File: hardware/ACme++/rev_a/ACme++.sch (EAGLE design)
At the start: 92 parts, among them J1 AC-PLUG, J2 TC2030-CTX-NL, J3 WIRE_HOLE-14AWG, J4 WIRE_HOLE-14AWG, J5 WIRE_HOLE-14AWG, K1 S216S01F, Q1 STGD5NB120SZT4, Q2 FDV301N, U1 CC2538, U2 DS2411, U3 FM25LBTDFN-8, U4 ADE7753, U5 TXB0104RGY, U6 SR086SG-G, U7 TDA3664AT, X1 EPSON-FA-128, X2 FC-12M32.7680KA-A3, X3 ECS-35-17-5PX-TR

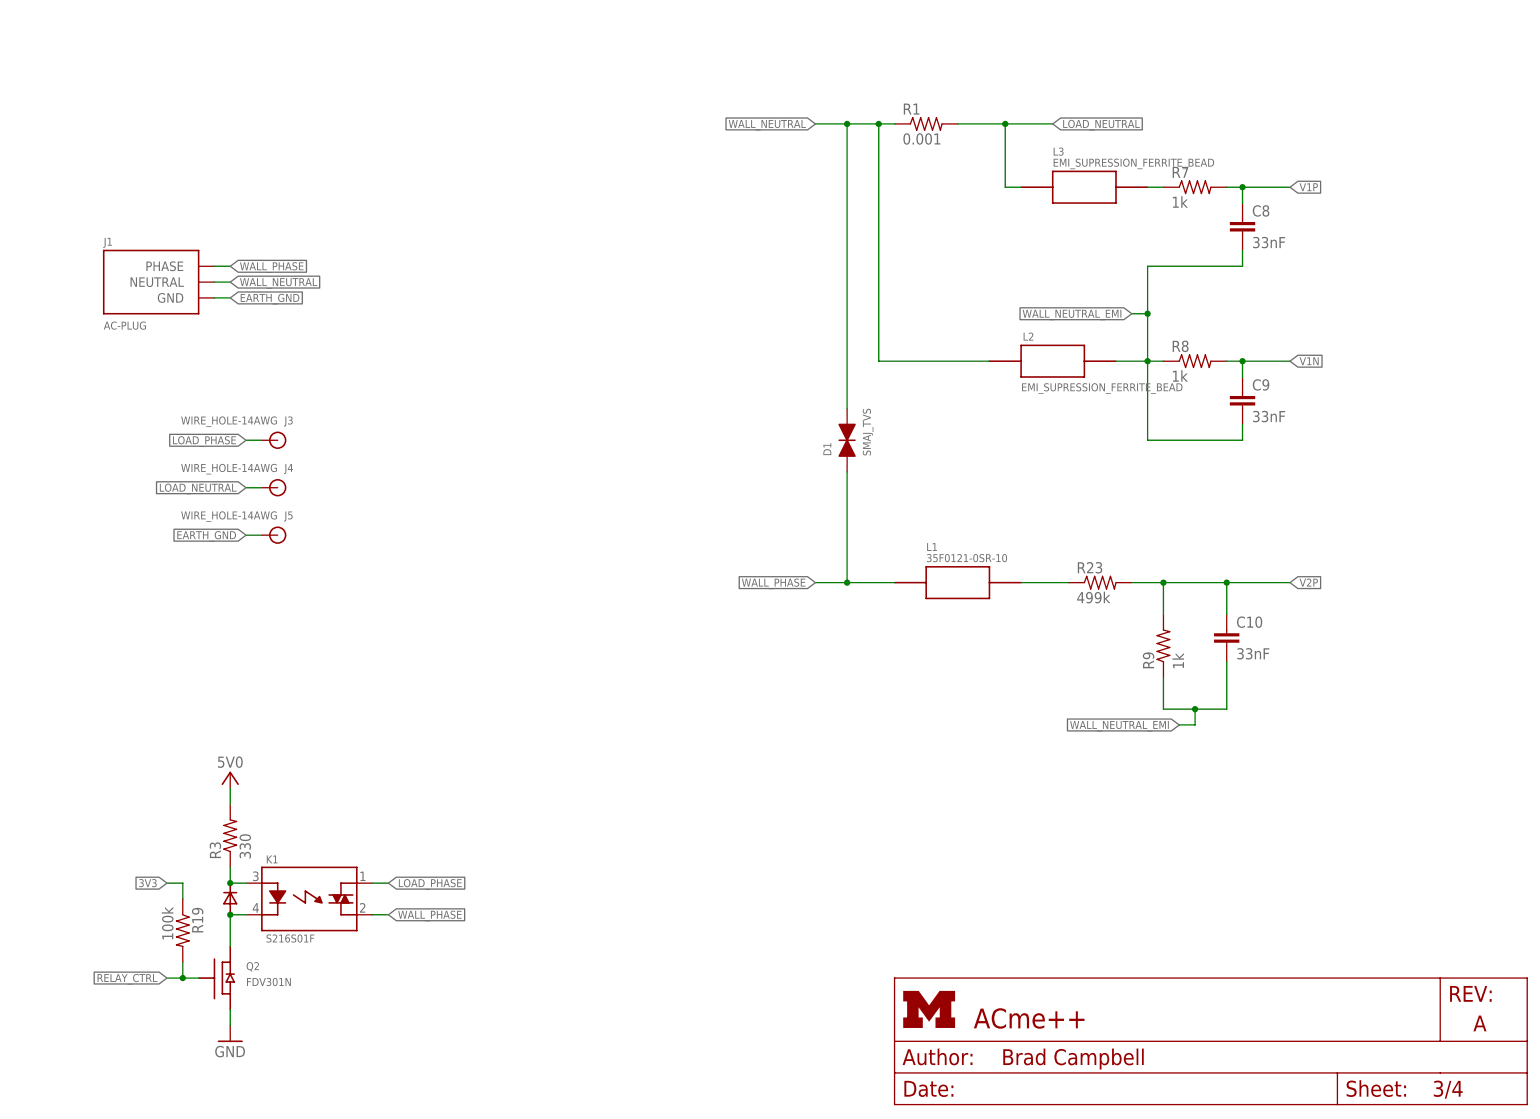
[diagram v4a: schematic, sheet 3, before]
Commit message: updates to acme++
- no plated earth gnd
- added test points
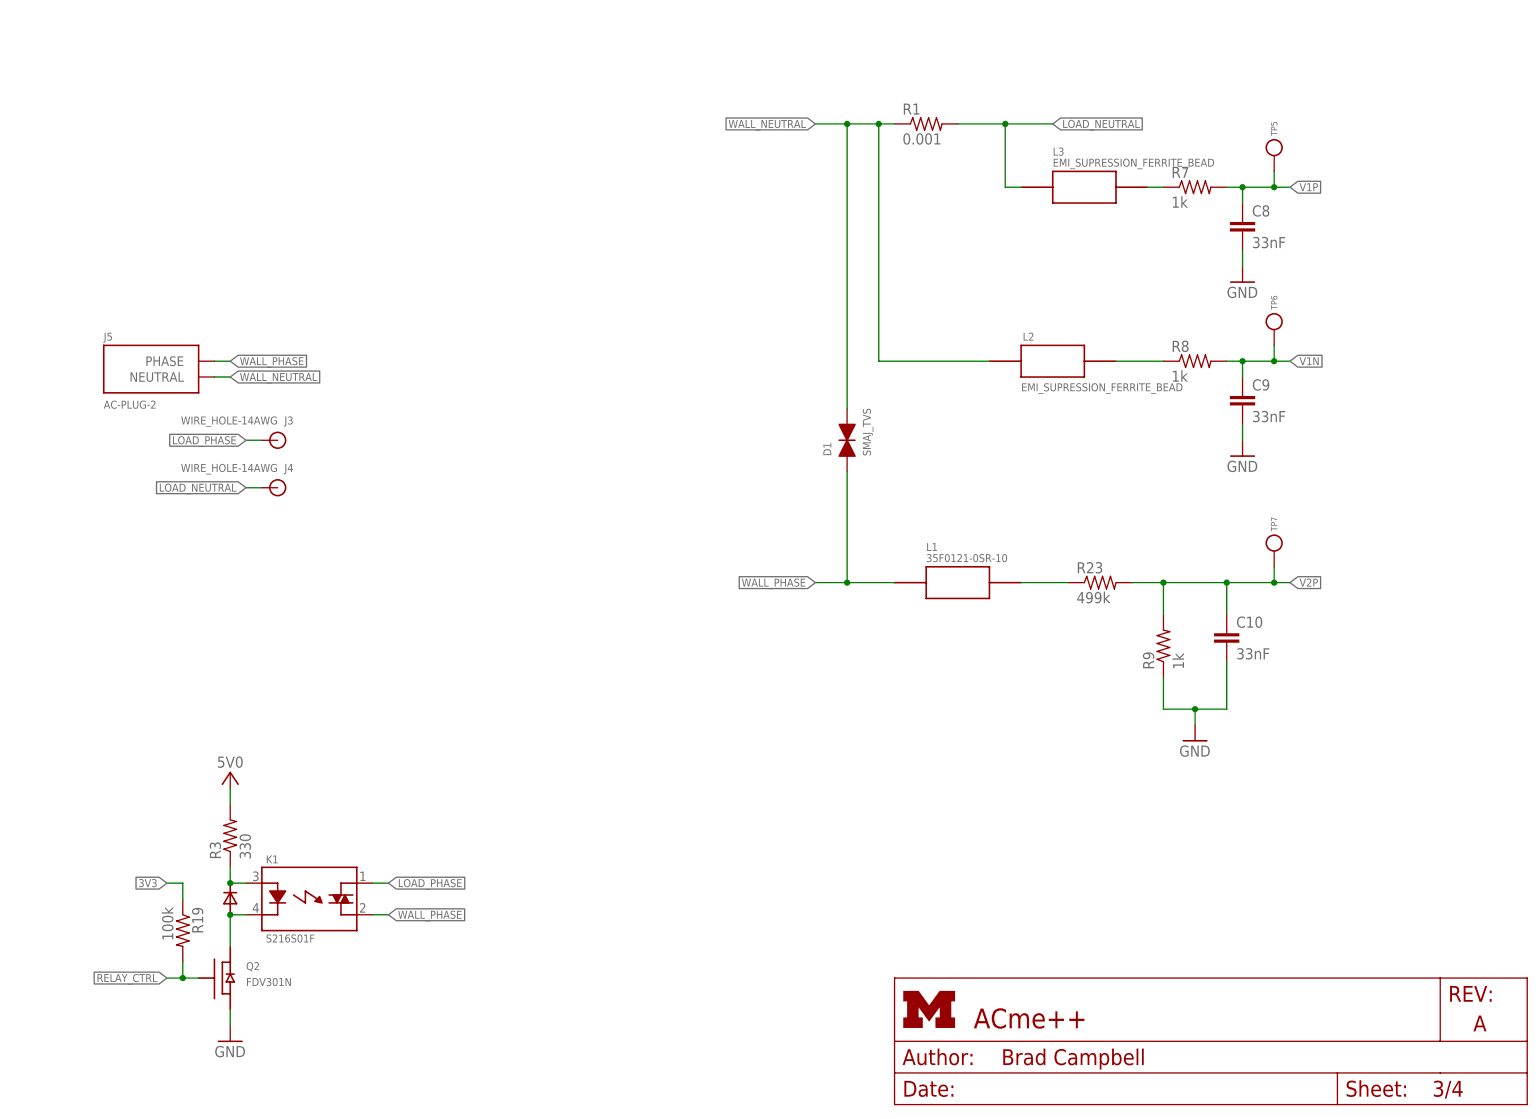
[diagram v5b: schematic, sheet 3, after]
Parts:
- removed C36, C37: (no value), powercube:CAP_POL
- removed J1: AC-PLUG, powercube:AC-PLUG
- added TP1, TP2, TP3, TP4, TP5, TP6, TP7: TEST_POINT_0.040IN, headers:TEST_POINT_0.040IN
- J5: value WIRE_HOLE-14AWG -> AC-PLUG-2; device powercube:WIRE_HOLE-14AWG -> powercube:AC-PLUG-2
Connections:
- removed net EARTH_GND: J1.GND, J5.P$1
- removed net WALL_NEUTRAL_EMI: C10.2, C8.2, C9.2, L2.P$2, R8.1, R9.1
- new net N$14: L2.P$2, R8.1
- net !ADE_CS: now also TP4.TESTPOINT
- net GND: now also C10.2, C8.2, C9.2, R9.1
- net MISO: now also TP2.TESTPOINT
- net MOSI: now also TP1.TESTPOINT
- net SCLK: now also TP3.TESTPOINT
- net V1N: now also TP6.TESTPOINT
- net V1P: now also TP5.TESTPOINT
- net V2P: now also TP7.TESTPOINT
- net WALL_NEUTRAL: now also J5.NEUTRAL; no longer J1.NEUTRAL
- net WALL_PHASE: now also J5.PHASE; no longer J1.PHASE

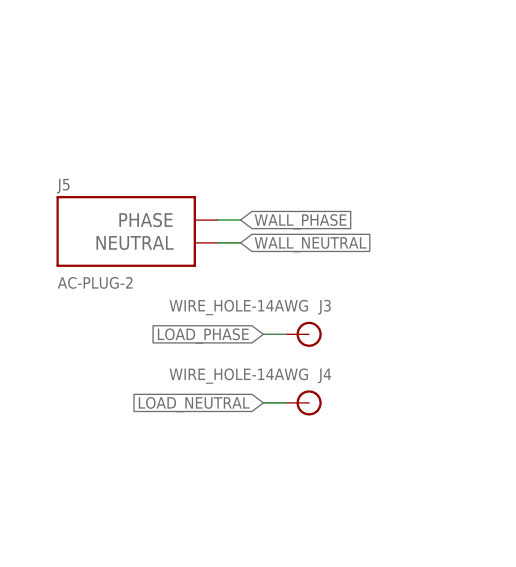
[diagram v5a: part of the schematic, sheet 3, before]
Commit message: worked on plated cutouts...
I hope sunstone will do something reasonable
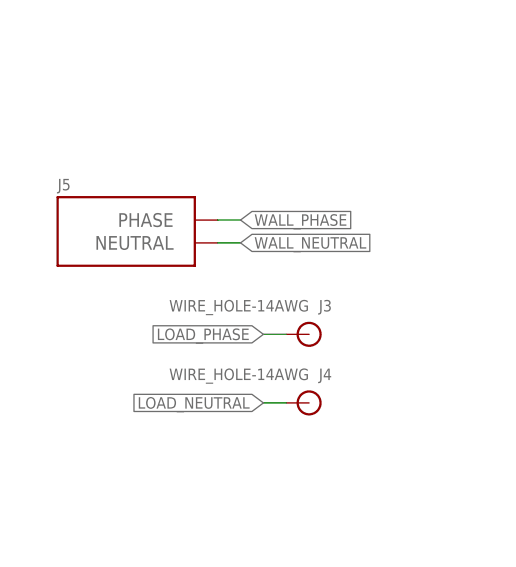
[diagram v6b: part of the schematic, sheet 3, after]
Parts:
- J5: value AC-PLUG-2 -> (none)
